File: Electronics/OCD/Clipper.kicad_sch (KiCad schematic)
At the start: 36 parts, among them U1 TL074H, U2 TL074H

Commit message: silkscreen pdf and schematic update to center-negative
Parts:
- C10, C4, C5, C7, C8, C9: footprint (none) -> Capacitor_SMD:C_0805_2012Metric
- R10, R11, R12, R13, R14, R15, R23, R24, R25, R26, R27, R28, R29, R30, R31, R6, R7, R8, R9: footprint (none) -> Resistor_SMD:R_0805_2012Metric
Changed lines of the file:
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@@
 			)
 		)
-		(property "Footprint" ""
+		(property "Footprint" "Resistor_SMD:R_0805_2012Metric"
 			(at 131.064 132.334 90)
 			(effects
@@
 			)
 		)
-		(property "Footprint" ""
+		(property "Footprint" "Resistor_SMD:R_0805_2012Metric"
 			(at 297.434 185.166 90)
 			(effects
@@
 			)
 		)
-		(property "Footprint" ""
+		(property "Footprint" "Resistor_SMD:R_0805_2012Metric"
 			(at 68.834 129.794 90)
 			(effects
@@
 			)
 		)
-		(property "Footprint" ""
+		(property "Footprint" "Resistor_SMD:R_0805_2012Metric"
 			(at 115.824 159.004 90)
 			(effects
@@
 			)
 		)
-		(property "Footprint" ""
+		(property "Footprint" "Resistor_SMD:R_0805_2012Metric"
 			(at 175.514 199.136 90)
 			(effects
@@
 			)
 		)
-		(property "Footprint" ""
+		(property "Footprint" "Resistor_SMD:R_0805_2012Metric"
 			(at 255.524 81.534 90)
 			(effects
@@
 			)
 		)
-		(property "Footprint" ""
+		(property "Footprint" "Resistor_SMD:R_0805_2012Metric"
 			(at 308.356 163.576 90)
 			(effects
@@
 			)
 		)
-		(property "Footprint" ""
+		(property "Footprint" "Capacitor_SMD:C_0805_2012Metric"
 			(at 321.31 136.8552 0)
 			(effects
@@
 			)
 		)
-		(property "Footprint" ""
+		(property "Footprint" "Resistor_SMD:R_0805_2012Metric"
 			(at 115.824 132.334 90)
 			(effects
@@
 			)
 		)
-		(property "Footprint" ""
+		(property "Footprint" "Resistor_SMD:R_0805_2012Metric"
 			(at 324.866 149.606 90)
 			(effects
@@
 			)
 		)
-		(property "Footprint" ""
+		(property "Footprint" "Capacitor_SMD:C_0805_2012Metric"
 			(at 73.66 119.0752 0)
 			(effects
@@
 			)
 		)
-		(property "Footprint" ""
+		(property "Footprint" "Resistor_SMD:R_0805_2012Metric"
 			(at 297.434 172.466 90)
 			(effects
@@
 			)
 		)
-		(property "Footprint" ""
+		(property "Footprint" "Resistor_SMD:R_0805_2012Metric"
 			(at 200.914 128.524 90)
 			(effects
@@
 			)
 		)
-		(property "Footprint" ""
+		(property "Footprint" "Capacitor_SMD:C_0805_2012Metric"
 			(at 76.5048 134.62 0)
 			(effects
@@
 			)
 		)
-		(property "Footprint" ""
+		(property "Footprint" "Resistor_SMD:R_0805_2012Metric"
 			(at 223.774 159.004 90)
 			(effects
@@
 			)
 		)
-		(property "Footprint" ""
+		(property "Footprint" "Resistor_SMD:R_0805_2012Metric"
 			(at 56.134 129.794 90)
 			(effects
@@
 			)
 		)
-		(property "Footprint" ""
+		(property "Footprint" "Resistor_SMD:R_0805_2012Metric"
 			(at 147.574 117.094 90)
 			(effects
@@
 			)
 		)
-		(property "Footprint" ""
+		(property "Footprint" "Resistor_SMD:R_0805_2012Metric"
 			(at 148.844 156.464 90)
 			(effects
@@
 			)
 		)
-		(property "Footprint" ""
+		(property "Footprint" "Resistor_SMD:R_0805_2012Metric"
 			(at 167.894 156.464 90)
 			(effects
@@
 			)
 		)
-		(property "Footprint" ""
+		(property "Footprint" "Resistor_SMD:R_0805_2012Metric"
 			(at 120.904 167.386 90)
 			(effects
@@
 			)
 		)
-		(property "Footprint" ""
+		(property "Footprint" "Capacitor_SMD:C_0805_2012Metric"
 			(at 191.4652 201.93 0)
 			(effects
@@
 			)
 		)
-		(property "Footprint" ""
+		(property "Footprint" "Resistor_SMD:R_0805_2012Metric"
 			(at 167.894 117.094 90)
 			(effects
@@
 			)
 		)
-		(property "Footprint" ""
+		(property "Footprint" "Resistor_SMD:R_0805_2012Metric"
 			(at 175.514 178.816 90)
 			(effects
@@
 			)
 		)
-		(property "Footprint" ""
+		(property "Footprint" "Capacitor_SMD:C_0805_2012Metric"
 			(at 246.38 69.5452 0)
 			(effects
@@
 			)
 		)
-		(property "Footprint" ""
+		(property "Footprint" "Capacitor_SMD:C_0805_2012Metric"
 			(at 196.85 143.2052 0)
 			(effects

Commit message: RevA release
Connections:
- net at D5.1 (K), RV4.3B: now also D4.2 (A); no longer D4.1 (K)
- net at C8.2, D2.2 (A), D3.1 (K)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: now also D4.1 (K); no longer D4.2 (A)
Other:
- moved on the sheet: D4

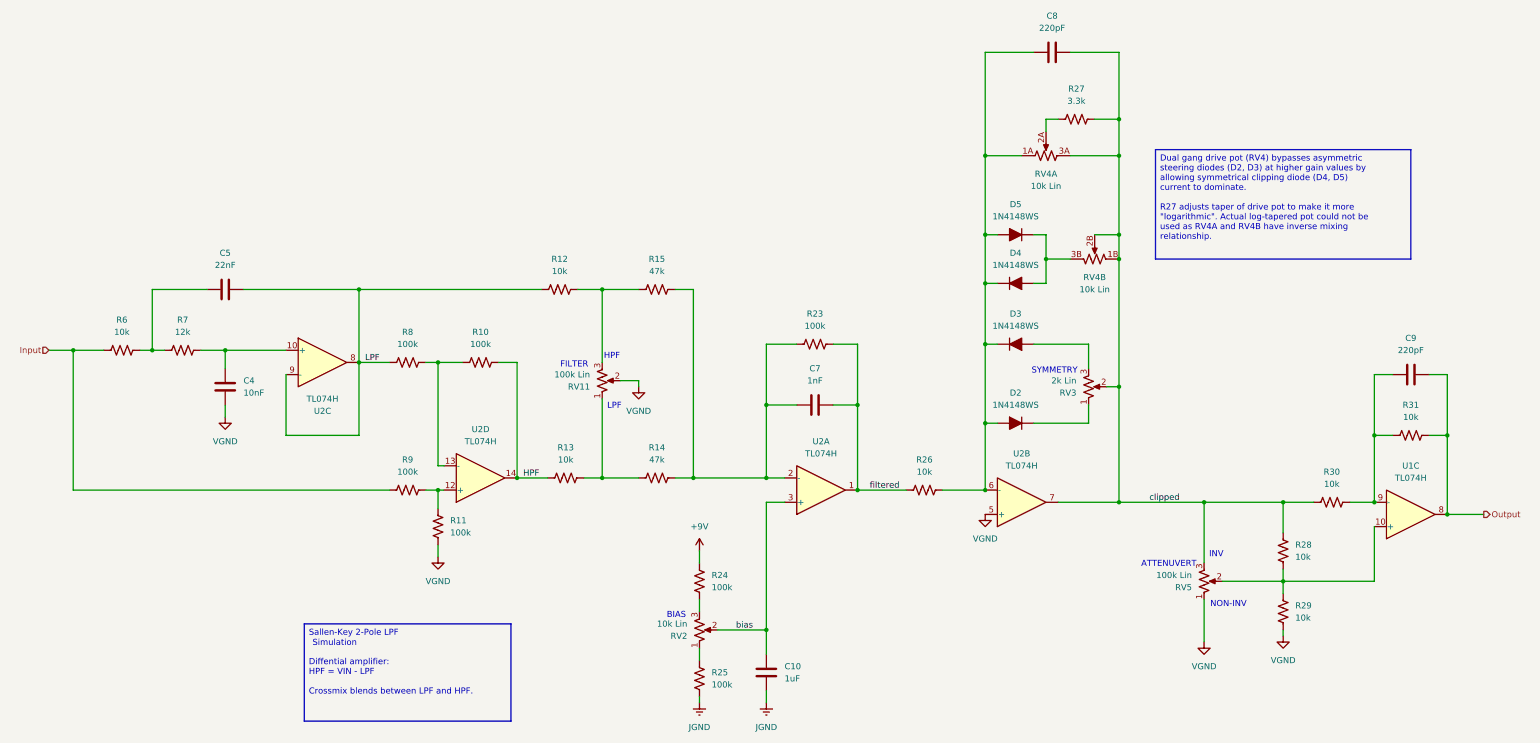
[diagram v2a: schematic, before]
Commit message: RevB release. Corrected opamp orientation, added pad switch
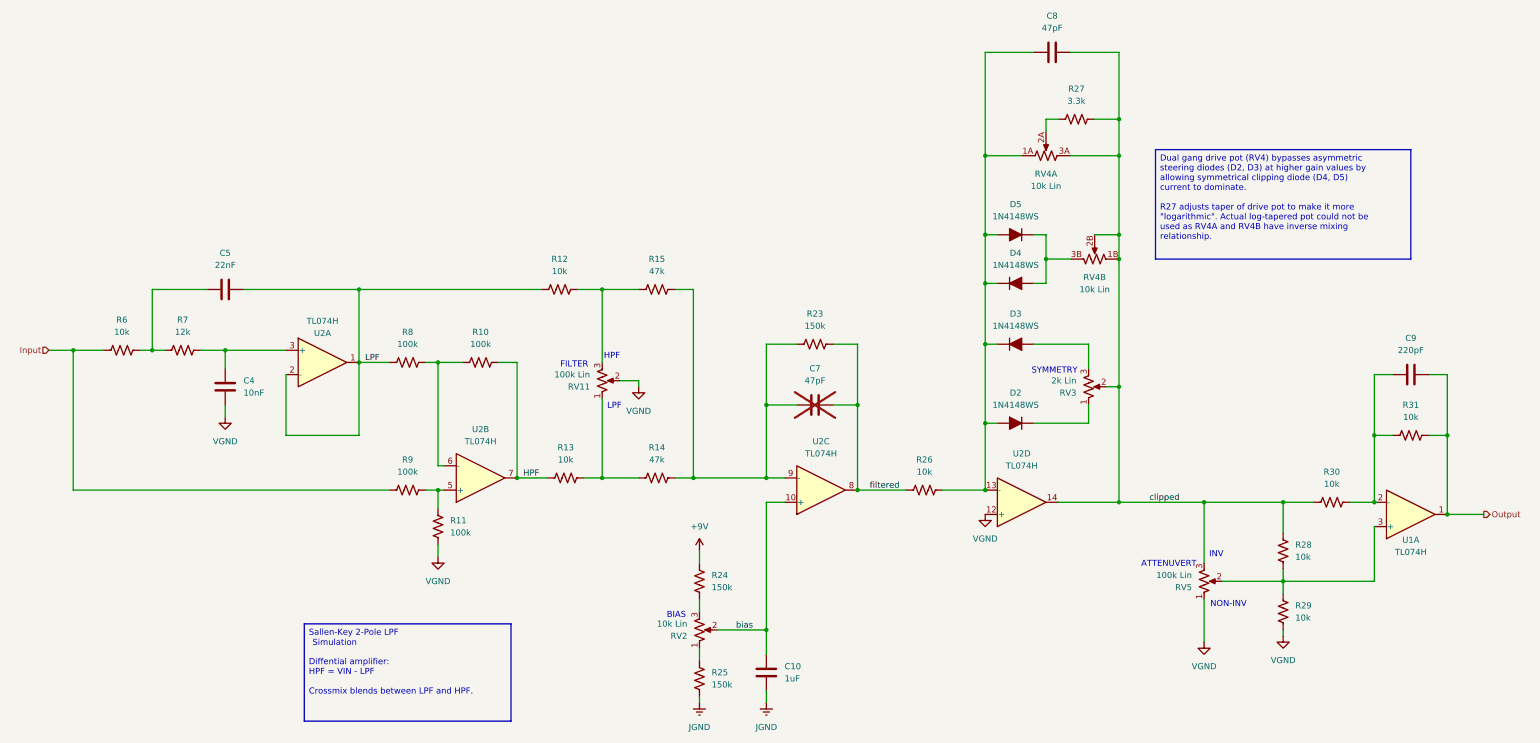
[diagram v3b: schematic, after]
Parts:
- removed U1: TL074H, Package_SO:SOIC-14_3.9x8.7mm_P1.27mm, symbol Amplifier_Operational:TL074
- added U1: TL074H, Package_SO:SOIC-14_3.9x8.7mm_P1.27mm, symbol Amplifier_Operational:TL074
- C10: Distributer (none) -> LCSC; Manufacturer (none) -> Samsung Electro-Mechanics; Part Number (none) -> CL21B105KBFNNNE; SKU (none) -> C28323
- C4: Distributer (none) -> LCSC; Manufacturer (none) -> Murata Electronics; Part Number (none) -> GRM2195C1H103JA01D; SKU (none) -> C97905
- C5: Distributer (none) -> LCSC; Manufacturer (none) -> Murata Electronics; Part Number (none) -> GRM21B5C1H223JA01L; SKU (none) -> C77069
- C7: value 1nF -> 47pF; Distributer (none) -> LCSC; Manufacturer (none) -> Samsung Electro-Mechanics; Part Number (none) -> CL21C470JBANNNC; SKU (none) -> C14857; now not fitted
- C8: value 220pF -> 47pF; Distributer (none) -> LCSC; Manufacturer (none) -> Samsung Electro-Mechanics; Part Number (none) -> CL21C470JBANNNC; SKU (none) -> C14857
- C9: Distributer (none) -> LCSC; Manufacturer (none) -> Samsung Electro-Mechanics; Part Number (none) -> CL21C221JBANNNC; SKU (none) -> C61747
- D2, D3, D4, D5: Distributer (none) -> LCSC; Manufacturer (none) -> ST(Semtech); Part Number (none) -> 1N4148WS; SKU (none) -> C57759
- R10, R11, R8, R9: Distributer (none) -> LCSC; Manufacturer (none) -> UNI-ROYAL(Uniroyal Elec); Part Number (none) -> 0805W8F1003T5E; SKU (none) -> C149504
- R12, R13, R26, R28, R29, R30, R31, R6: Distributer (none) -> LCSC; Manufacturer (none) -> UNI-ROYAL(Uniroyal Elec); Part Number (none) -> 0805W8F1002T5E; SKU (none) -> C17414
- R14, R15: Distributer (none) -> LCSC; Manufacturer (none) -> UNI-ROYAL(Uniroyal Elec); Part Number (none) -> 0805W8F4702T5E; SKU (none) -> C17713
- R23, R24, R25: value 100k -> 150k; Distributer (none) -> LCSC; Manufacturer (none) -> UNI-ROYAL(Uniroyal Elec); Part Number (none) -> 0805W8F1503T5E; SKU (none) -> C17470
- R27: Distributer (none) -> LCSC; Manufacturer (none) -> UNI-ROYAL(Uniroyal Elec); Part Number (none) -> 0805W8F3301T5E; SKU (none) -> C26010
- R7: Distributer (none) -> LCSC; Manufacturer (none) -> UNI-ROYAL(Uniroyal Elec); Part Number (none) -> 0805W8F1202T5E; SKU (none) -> C17444
- U2: Distributer (none) -> LCSC; SKU (none) -> C2878713
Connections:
- net HPF: now also U2.7; no longer U2.14
- net LPF: now also U2.1, U2.2 (-); no longer U2.8, U2.9 (-)
- net Output: now also U1.1
- net VGND: now also U2.12 (+); no longer U2.5 (+)
- net bias: now also U2.10 (+); no longer U2.3 (+)
- net clipped: now also U2.14; no longer U2.7
- net filtered: now also U2.8; no longer U2.1
- net at R10.1, R8.2: now also U2.6 (-); no longer U2.13 (-)
- net at R28.1, R29.2, RV5.2: now also U1.3 (+)
- net at C4.2, R7.2: now also U2.3 (+); no longer U2.10 (+)
- net at C8.2, D2.2 (A), D3.1 (K)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: now also U2.13 (-); no longer U2.6 (-)
- net at R11.2, R9.2: now also U2.5 (+); no longer U2.12 (+)
- net at C7.2, R14.2, R15.2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: now also U2.9 (-); no longer U2.2 (-)
- net at C9.2, R30.1, R31.2: now also U1.2 (-)
